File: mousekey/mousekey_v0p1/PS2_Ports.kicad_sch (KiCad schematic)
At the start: 14 parts

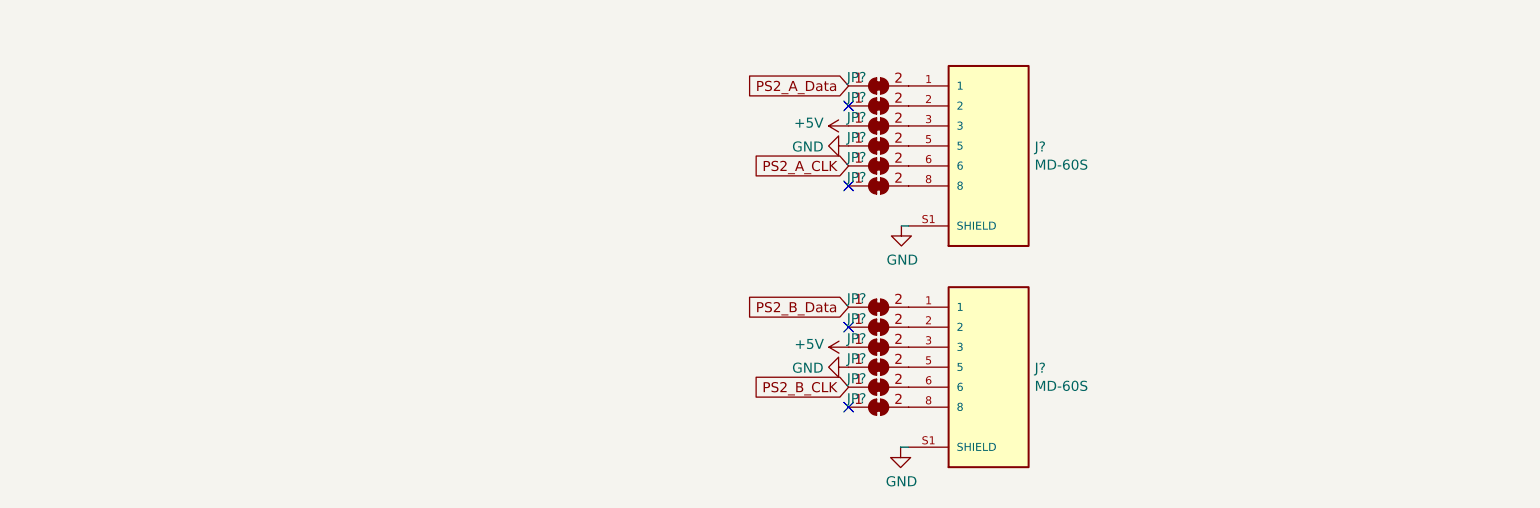
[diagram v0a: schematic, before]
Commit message: Added ADB and Teensy
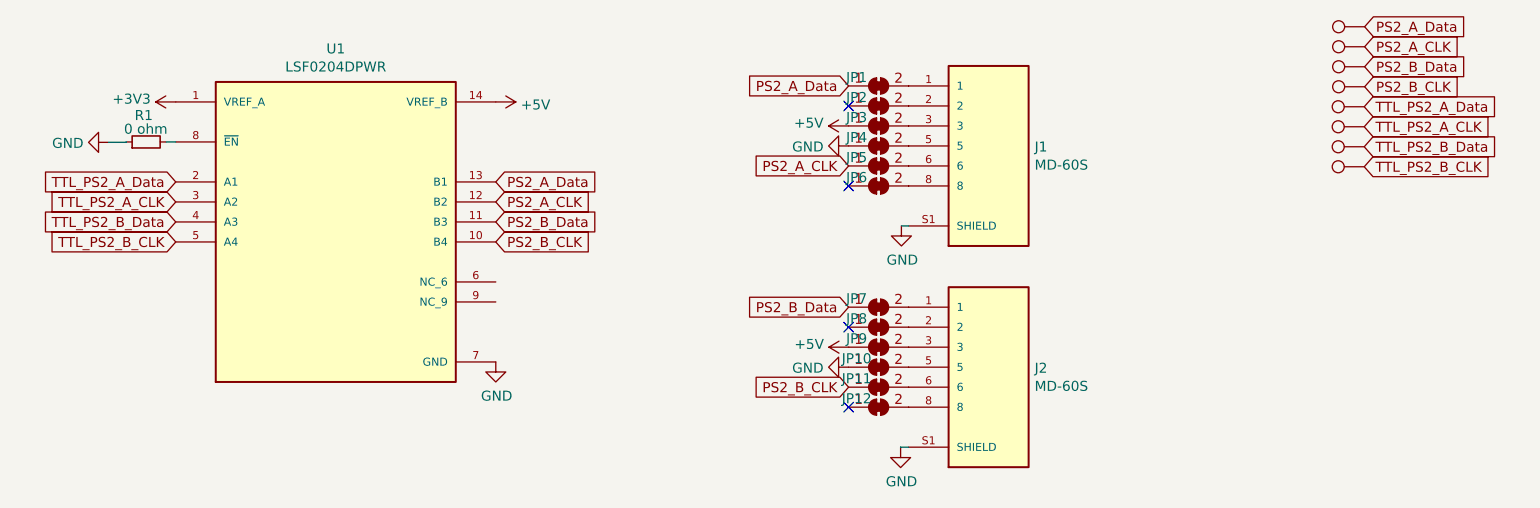
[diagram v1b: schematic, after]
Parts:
- added R1: 0 ohm, Resistor_SMD:R_0805_2012Metric, symbol Device:R_Small
- added TP10, TP11, TP12, TP13, TP14, TP15, TP16, TP9: TestPoint, TestPoint:TestPoint_THTPad_2.0x2.0mm_Drill1.0mm, symbol Connector:TestPoint
- added U1: LSF0204DPWR, SOP65P640X120-14N, symbol LSF0204DPWR:LSF0204DPWR
- gave numbers to parts that had none: 14
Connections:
- net +5V: now also U1.14 (VREF_B)
- net GND: now also R1.1, U1.7 (GND)
- net PS2_A_CLK: now also TP14.1, U1.12 (B2)
- net PS2_A_Data: now also TP13.1, U1.13 (B1)
- net PS2_B_CLK: now also TP16.1, U1.10 (B4)
- net PS2_B_Data: now also TP15.1, U1.11 (B3)
- new net: R1.2, U1.8 (~EN)
- new net +3V3: U1.1 (VREF_A)
- new net TTL_PS2_A_CLK: TP10.1, U1.3 (A2)
- new net TTL_PS2_A_Data: TP9.1, U1.2 (A1)
- new net TTL_PS2_B_CLK: TP12.1, U1.5 (A4)
- new net TTL_PS2_B_Data: TP11.1, U1.4 (A3)
